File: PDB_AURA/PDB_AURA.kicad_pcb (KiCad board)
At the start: 4 copper layers, 50 x 50 mm, 76 parts, among them J100 XT30PW-M, J200 532617010, J201 XT30PW-F, J202 XT30PW-F, J203 XT30PW-F, J204 XT30PW-F, Q1 CSD18540Q5B, Q2 CSD18510Q5B, Q200 HSK10N06, Q201 HSK10N06, Q3 CSD18540Q5B, U1 LM25145RGYR, U2 LM74700, U200 LTV-217-B-G, U201 LTV-217-B-G, U202 INA219AIDCNR

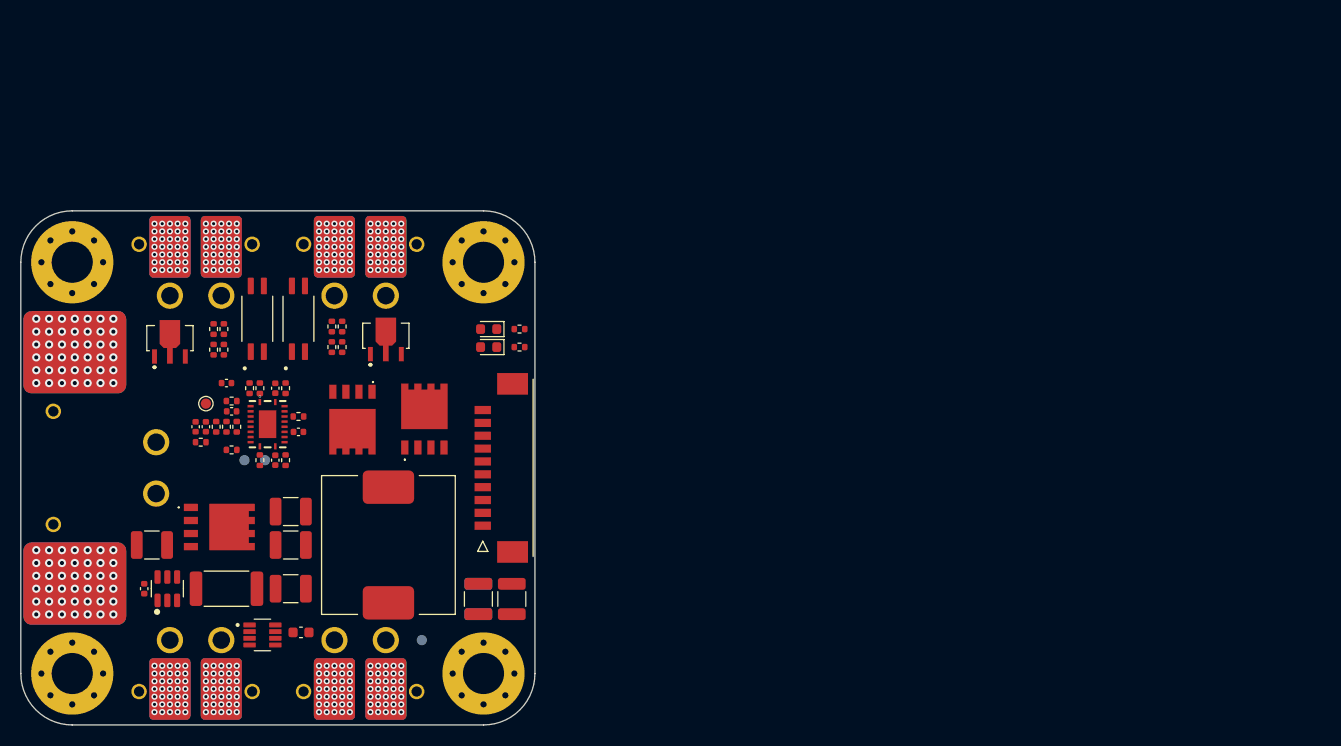
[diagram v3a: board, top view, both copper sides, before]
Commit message: Annotated schematic for PDB
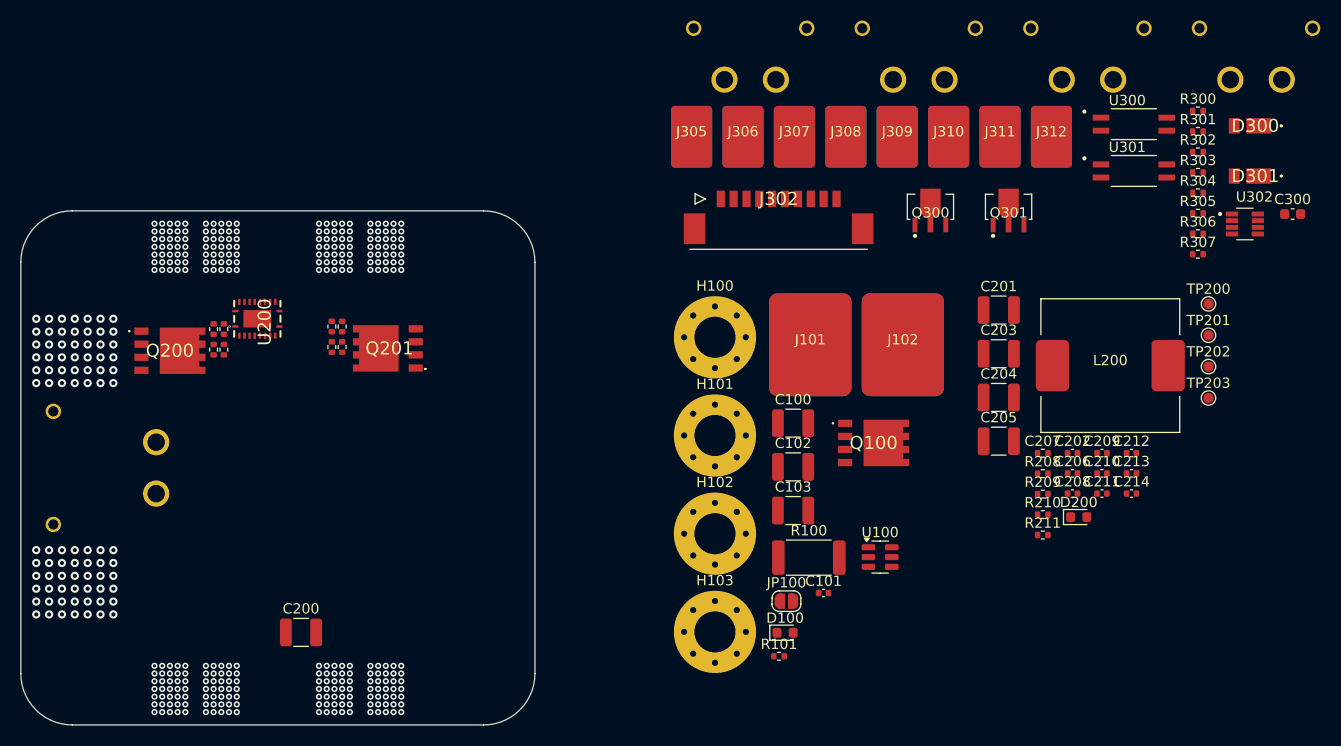
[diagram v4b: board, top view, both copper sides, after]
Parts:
- removed C1: 1n, Capacitor_SMD:C_0402_1005Metric
- removed C10: 47u, Capacitor_SMD:C_1210_3225Metric
- removed C11, C12, C14, C15, C16, C9: 22u, Capacitor_SMD:C_1210_3225Metric
- removed C2: 8n2, Capacitor_SMD:C_0402_1005Metric
- removed C3, C8: 100n, Capacitor_SMD:C_0402_1005Metric
- removed C4 (x2): 390p, Capacitor_SMD:C_0402_1005Metric
- removed C5: 100n, Resistor_SMD:R_0402_1005Metric
- removed C6: 2u2, Capacitor_SMD:C_0402_1005Metric
- removed C7: 10p, Capacitor_SMD:C_0402_1005Metric
- removed D1, D101: LED, LED_SMD:LED_0603_1608Metric
- removed H1, H2, H3, H4: MountingHole_Pad, MountingHole:MountingHole_4mm_Pad_Via
- removed J1, J2, J3, J4, J5, J6, J7, J8: ~, SOLDER_PAD:PWR_SOLDER_PAD
- removed J10, J9: ~, SOLDER_PAD:BAT_SOLDER_PAD
- removed J200: 532617010, 532617010:532617010
- removed J201, J202, J203, J204: XT30PW-F, XT30PWF:XT30PWF
- removed L1: 1u8, 125CDMCCDS-1R8MC:Untitled
- removed Q1, Q3: CSD18540Q5B, CSD18540Q5B:CSD18540Q5B
- removed Q2: CSD18510Q5B, CSD18510Q5B:CSD18540Q5BT
- removed R1: 18k, Resistor_SMD:R_0402_1005Metric
- removed R10: 9k1, Resistor_SMD:R_0402_1005Metric
- removed R11: 2R1, Resistor_SMD:R_0402_1005Metric
- removed R112, R13, R4, R8: 4k7, Resistor_SMD:R_0402_1005Metric
- removed R12: 0m5, Resistor_SMD:R_2512_6332Metric
- removed R2: 3k4, Resistor_SMD:R_0402_1005Metric
- removed R3: 1k47, Resistor_SMD:R_0402_1005Metric
- removed R5: 249R, Resistor_SMD:R_0402_1005Metric
- removed R6: 20k, Resistor_SMD:R_0402_1005Metric
- removed R7: 576R, Resistor_SMD:R_0402_1005Metric
- removed R9: 35k7, Resistor_SMD:R_0402_1005Metric
- removed TP1, TP2, TP3, TP4: TestPoint, TestPoint:TestPoint_Pad_D1.0mm
- removed U1: LM25145RGYR, LM24145RGYR:RGY0020B
- removed U2: LM74700, Package_TO_SOT_SMD:SOT-23-6
- removed U201: LTV-217-B-G, LTV-217-B-G:SOIC127P700X210-4N
- removed U202: INA219AIDCNR, INA219AIDCNR:SOT65P280X145-8N
- added C100: 22u, Capacitor_SMD:C_1210_3225Metric, F.Cu at (125.1, 70.7)
- added C101: 47n, Capacitor_SMD:C_0402_1005Metric, F.Cu at (128.1, 87.2)
- added C102: 22u, Capacitor_SMD:C_1210_3225Metric, F.Cu at (125.1, 74.9)
- added C103: 22u, Capacitor_SMD:C_1210_3225Metric, F.Cu at (125.1, 79.2)
- added C201: 22u, Capacitor_SMD:C_1210_3225Metric, F.Cu at (145.1, 59.6)
- added C202: 100n, Capacitor_SMD:C_0402_1005Metric, F.Cu at (152.3, 73.6)
- added C203: 22u, Capacitor_SMD:C_1210_3225Metric, F.Cu at (145.1, 63.9)
- added C204: 22u, Capacitor_SMD:C_1210_3225Metric, F.Cu at (145.1, 68.2)
- added C205: 22u, Capacitor_SMD:C_1210_3225Metric, F.Cu at (145.1, 72.4)
- added C206: 100n, Capacitor_SMD:C_0402_1005Metric, F.Cu at (152.3, 75.5)
- added C207: 100n, Resistor_SMD:R_0402_1005Metric, F.Cu at (149.4, 73.6)
- added C208: 100n, Capacitor_SMD:C_0402_1005Metric, F.Cu at (152.3, 77.5)
- added C209: 2u2, Capacitor_SMD:C_0402_1005Metric, F.Cu at (155.2, 73.6)
- added C210: 10p, Capacitor_SMD:C_0402_1005Metric, F.Cu at (155.2, 75.5)
- added C211: 100n, Capacitor_SMD:C_0402_1005Metric, F.Cu at (155.2, 77.5)
- added C212: 1n, Capacitor_SMD:C_0402_1005Metric, F.Cu at (158.0, 73.6)
- added C213: 8n2, Capacitor_SMD:C_0402_1005Metric, F.Cu at (158.0, 75.5)
- added C214: 390p, Capacitor_SMD:C_0402_1005Metric, F.Cu at (158.0, 77.5)
- added C300: 100n, Capacitor_SMD:C_0603_1608Metric, F.Cu at (173.7, 50.3)
- added D100: LED, LED_SMD:LED_0603_1608Metric, F.Cu at (124.3, 91.0)
- added D200: LED, LED_SMD:LED_0603_1608Metric, F.Cu at (152.9, 79.8)
- added D300: SBR3M30P17, SBR3M30P17:SBR3M30P17, F.Cu at (169.5, 41.7)
- added D301: SBR3M30P17, SBR3M30P17:SBR3M30P17, F.Cu at (169.5, 46.6)
- added H100: MountingHole_Pad, MountingHole:MountingHole_4mm_Pad_Via, F.Cu at (117.5, 62.3)
- added H101: MountingHole_Pad, MountingHole:MountingHole_4mm_Pad_Via, F.Cu at (117.5, 71.8)
- added H102: MountingHole_Pad, MountingHole:MountingHole_4mm_Pad_Via, F.Cu at (117.5, 81.4)
- added H103: MountingHole_Pad, MountingHole:MountingHole_4mm_Pad_Via, F.Cu at (117.5, 91.0)
- added J101: ~, SOLDER_PAD:BAT_SOLDER_PAD, F.Cu at (126.8, 63.0)
- added J102: ~, SOLDER_PAD:BAT_SOLDER_PAD, F.Cu at (135.8, 63.0)
- added J300: XT30PW-F, XT30PWF:XT30PWF, F.Cu at (118.4, 37.2)
- added J301: XT30PW-F, XT30PWF:XT30PWF, F.Cu at (134.8, 37.2)
- added J302: 532617010, 532617010:532617010, F.Cu at (123.7, 48.8)
- added J303: XT30PW-F, XT30PWF:XT30PWF, F.Cu at (151.2, 37.2)
- added J304: XT30PW-F, XT30PWF:XT30PWF, F.Cu at (167.6, 37.2)
- added J305: ~, SOLDER_PAD:PWR_SOLDER_PAD, F.Cu at (115.2, 42.8)
- added J306: ~, SOLDER_PAD:PWR_SOLDER_PAD, F.Cu at (120.2, 42.8)
- added J307: ~, SOLDER_PAD:PWR_SOLDER_PAD, F.Cu at (125.2, 42.8)
- added J308: ~, SOLDER_PAD:PWR_SOLDER_PAD, F.Cu at (130.2, 42.8)
- added J309: ~, SOLDER_PAD:PWR_SOLDER_PAD, F.Cu at (135.2, 42.8)
- added J310: ~, SOLDER_PAD:PWR_SOLDER_PAD, F.Cu at (140.2, 42.8)
- added J311: ~, SOLDER_PAD:PWR_SOLDER_PAD, F.Cu at (145.2, 42.8)
- added J312: ~, SOLDER_PAD:PWR_SOLDER_PAD, F.Cu at (150.2, 42.8)
- added JP100: SolderJumper_2_Open, Jumper:SolderJumper-2_P1.3mm_Open_RoundedPad1.0x1.5mm, F.Cu at (124.5, 88.0)
- added L200: 1u8, 125CDMCCDS-1R8MC:Untitled, F.Cu at (156.0, 65.0)
- added Q100: CSD18540Q5B, CSD18540Q5B:CSD18540Q5B, F.Cu at (132.9, 72.6)
- added Q300: HSK10N06, HSK10N06:HSK10N06, F.Cu at (138.5, 50.8)
- added Q301: HSK10N06, HSK10N06:HSK10N06, F.Cu at (146.1, 50.8)
- added R100: 0m5, Resistor_SMD:R_2512_6332Metric, F.Cu at (126.6, 83.7)
- added R101: 4k7, Resistor_SMD:R_0402_1005Metric, F.Cu at (123.7, 93.3)
- added R208: 4k7, Resistor_SMD:R_0402_1005Metric, F.Cu at (149.4, 75.6)
- added R209: 4k7, Resistor_SMD:R_0402_1005Metric, F.Cu at (149.4, 77.5)
- added R210: 576R, Resistor_SMD:R_0402_1005Metric, F.Cu at (149.4, 79.5)
- added R211: 4k7, Resistor_SMD:R_0402_1005Metric, F.Cu at (149.4, 81.5)
- added R300: 10k, Resistor_SMD:R_0402_1005Metric, F.Cu at (164.5, 40.3)
- added R301: 220R, Resistor_SMD:R_0402_1005Metric, F.Cu at (164.5, 42.3)
- added R302: 10k, Resistor_SMD:R_0402_1005Metric, F.Cu at (164.5, 44.3)
- added R303: 100R, Resistor_SMD:R_0402_1005Metric, F.Cu at (164.5, 46.3)
- added R304: 10k, Resistor_SMD:R_0402_1005Metric, F.Cu at (164.5, 48.2)
- added R305: 220R, Resistor_SMD:R_0402_1005Metric, F.Cu at (164.5, 50.2)
- added R306: 10k, Resistor_SMD:R_0402_1005Metric, F.Cu at (164.5, 52.2)
- added R307: 100R, Resistor_SMD:R_0402_1005Metric, F.Cu at (164.5, 54.2)
- added TP200: TestPoint, TestPoint:TestPoint_Pad_D1.0mm, F.Cu at (165.5, 59.0)
- added TP201: TestPoint, TestPoint:TestPoint_Pad_D1.0mm, F.Cu at (165.5, 62.1)
- added TP202: TestPoint, TestPoint:TestPoint_Pad_D1.0mm, F.Cu at (165.5, 65.2)
- added TP203: TestPoint, TestPoint:TestPoint_Pad_D1.0mm, F.Cu at (165.5, 68.2)
- added U100: LM74700, Package_TO_SOT_SMD:SOT-23-6, F.Cu at (133.6, 83.7)
- added U300: LTV-217-B-G, LTV-217-B-G:SOIC127P700X210-4N, F.Cu at (158.2, 41.6)
- added U301: LTV-217-B-G, LTV-217-B-G:SOIC127P700X210-4N, F.Cu at (158.2, 46.1)
- added U302: INA219AIDCNR, INA219AIDCNR:SOT65P280X145-8N, F.Cu at (169.1, 51.3)
- C200: value 100n -> 47u; footprint Capacitor_SMD:C_0603_1608Metric -> Capacitor_SMD:C_1210_3225Metric
- Q200: value HSK10N06 -> CSD18540Q5B; footprint HSK10N06:HSK10N06 -> CSD18540Q5B:CSD18540Q5B
- Q201: value HSK10N06 -> CSD18510Q5B; footprint HSK10N06:HSK10N06 -> CSD18510Q5B:CSD18540Q5BT
- R200: value 10k -> 2R1
- R201: value 470R -> 35k7
- R202: value 10k -> 9k1
- R203: value 100R -> 20k
- R204: value 10k -> 249R
- R205: value 470R -> 3k4
- R206: value 10k -> 18k
- R207: value 100R -> 1k47
- U200: value LTV-217-B-G -> LM25145RGYR; footprint LTV-217-B-G:SOIC127P700X210-4N -> LM24145RGYR:RGY0020B
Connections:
- C200 pad 1: +3V3 -> +BATT_FILT
- Q200 pad 1: /200_Connectors/VGS_CH1_R -> /200_Buck_Regulator/5V_HO
- Q200 pad 2: /200_Connectors/VBAT_CH1 -> +BATT_FILT
- Q200 pad 3: GND -> /200_Buck_Regulator/5V_SW
- Q201 pad 1: /200_Connectors/VGS_CH2_R -> /200_Buck_Regulator/5V_LO
- Q201 pad 2: /200_Connectors/VBAT_CH2 -> /200_Buck_Regulator/5V_SW
- R200 pad 1: GND -> /200_Buck_Regulator/5V_VIN
- R200 pad 2: MSFT_1 -> +BATT_FILT
- R201 pad 1: /200_Connectors/MSFT_1_R -> /200_Buck_Regulator/5V_EN
- R201 pad 2: MSFT_1 -> +BATT_FILT
- R202 pad 2: /200_Connectors/VGS_CH1 -> /200_Buck_Regulator/5V_EN
- R203 pad 1: /200_Connectors/VGS_CH1_R -> /200_Buck_Regulator/5V_SYNCIN
- R203 pad 2: /200_Connectors/VGS_CH1 -> +5V_VCC
- R204 pad 1: GND -> /200_Buck_Regulator/5V_FB_RC
- R204 pad 2: MSFT_2 -> +5V
- R205 pad 1: /200_Connectors/MSFT_2_R -> GND
- R205 pad 2: MSFT_2 -> /200_Buck_Regulator/5V_FB
- R206 pad 1: GND -> /200_Buck_Regulator/5V_FB
- R206 pad 2: /200_Connectors/VGS_CH2 -> +5V
- R207 pad 1: /200_Connectors/VGS_CH2_R -> /200_Buck_Regulator/5V_FB
- R207 pad 2: /200_Connectors/VGS_CH2 -> /200_Buck_Regulator/COMP_FB_R
- U200 pad 1: /200_Connectors/MSFT_1_R -> /200_Buck_Regulator/5V_EN
- U200 pad 2: GND -> /200_Buck_Regulator/5V_RT
- U200 pad 3: /200_Connectors/VGS_CH1 -> /200_Buck_Regulator/5V_SS
- U200 pad 4: +5V -> /200_Buck_Regulator/COMP_FB_C

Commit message: Second Layout Attempt
Renamed all components and placed them all.
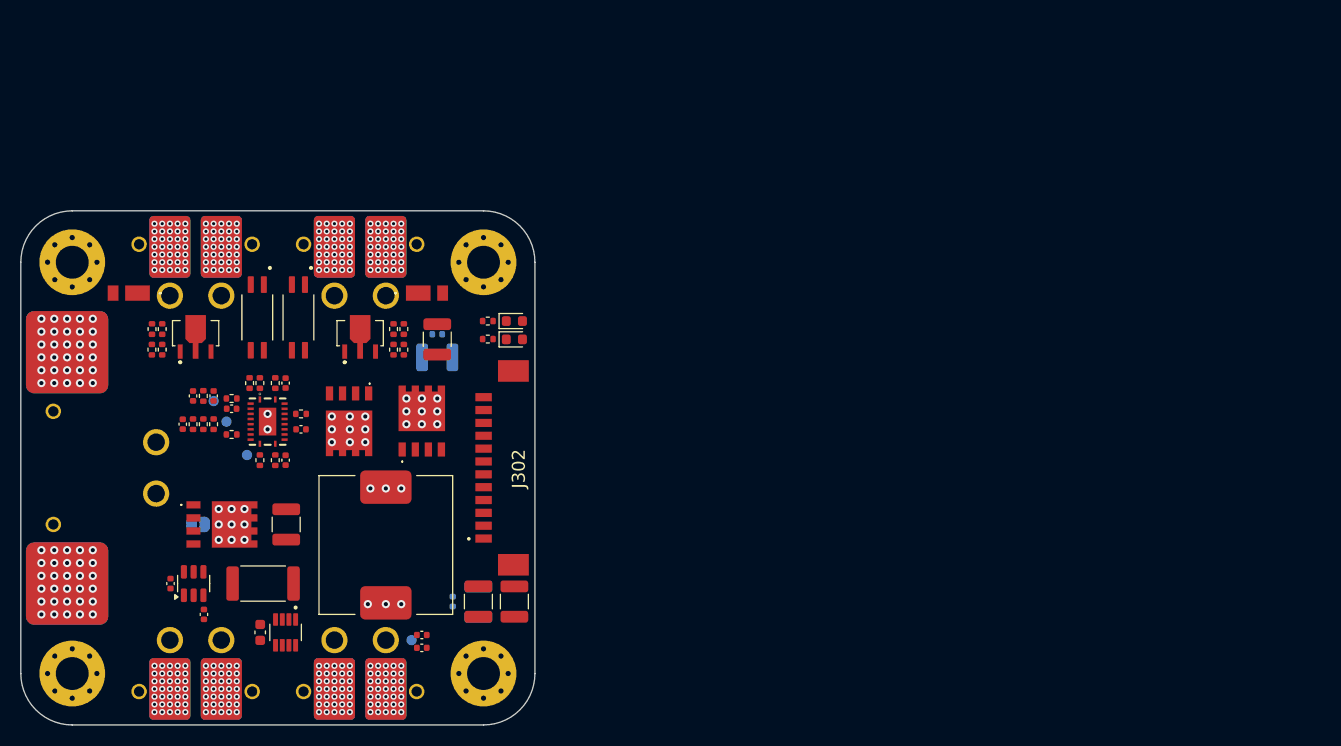
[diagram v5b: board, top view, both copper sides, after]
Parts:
- removed C100, C103: 22u, Capacitor_SMD:C_1210_3225Metric
- removed C206: 100n, Capacitor_SMD:C_0402_1005Metric
- added C104: 22n, Capacitor_SMD:C_0402_1005Metric, F.Cu at (67.8, 89.2)
- added C215: 100n, Capacitor_SMD:C_0402_1005Metric, B.Cu at (92.0, 88.0)
- added C216: 22u, Capacitor_SMD:C_1210_3225Metric, B.Cu at (94.5, 88.0)
- added C217: 100n, Capacitor_SMD:C_0402_1005Metric, B.Cu at (90.5, 62.0)
- added C218: 1u, Capacitor_SMD:C_0402_1005Metric, B.Cu at (90.5, 61.0)
- C102: value 22u -> 47u
- C201: value 22u -> 47u; moved to B.Cu
- C203: value 22u -> 1u; footprint Capacitor_SMD:C_1210_3225Metric -> Capacitor_SMD:C_0402_1005Metric
- H100, H101, H102, H103: footprint MountingHole:MountingHole_4mm_Pad_Via -> MountingHole:MountingHole_3.2mm_M3_Pad_Via
- J302: value 532617010 -> 532617012; footprint 532617010:532617010 -> 532611271:53261-1271
- J305, J306, J307, J308, J309, J310, J311, J312, JP100, TP200, TP201, TP202, TP203: moved to B.Cu
- moved D301 109.6 mm to (60.5, 58.0)
- moved C300 108.3 mm to (73.3, 91.0), turned to -90 degrees
- moved R300 104.3 mm to (62.8, 63.5), turned to -90 degrees
- moved R302 103.2 mm to (62.8, 61.5), turned to 90 degrees
- moved R301 102.9 mm to (63.8, 63.5), turned to -90 degrees
- moved R303 101.9 mm to (63.8, 61.5), turned to 90 degrees
- moved U302 101.4 mm to (75.8, 91.0), turned to -90 degrees
- moved J312 101.2 mm to (64.5, 96.5), turned to 180 degrees
- moved J304 98.6 mm to (85.5, 91.8), turned to 180 degrees
- moved J303 98.2 mm to (69.5, 91.8), turned to 180 degrees
- moved TP201 97.0 mm to (68.8, 68.5), turned to 180 degrees
- moved TP203 95.5 mm to (70.0, 70.5), turned to 180 degrees
- moved TP202 93.9 mm to (72.0, 73.8), turned to 180 degrees
- moved J311 92.8 mm to (69.5, 96.5), turned to 180 degrees
- moved C213 92.4 mm to (65.8, 70.8), turned to 90 degrees
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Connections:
- C202 pad 1: +BATT_FILT -> +5V
- J302 pad 11: (no net) -> GND
- J302 pad 12: (no net) -> GND
- J302 pad 3: +3V3 -> +5V
- J302 pad 4: SCL -> +3V3
- J302 pad 5: SDA -> SCL
- J302 pad 6: GND -> SDA
- J302 pad 7: MSFT_1 -> GND
- J302 pad 8: MSFT_2 -> MSFT_1
- J302 pad 9: GND -> MSFT_2
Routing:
- net INA_IN+: vias 0 -> 9
- net GND: vias 182 -> 172
- net /200_Buck_Regulator/5V_SW: vias 0 -> 12
- net +BATT_FILT: vias 140 -> 149
- net +BATT: vias 42 -> 30
- net +5V: vias 0 -> 3

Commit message: Started Routing
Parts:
- C201, C215, C216, C217: moved to F.Cu
- J302: moved to B.Cu
- moved C216 11.8 mm to (95.5, 76.2), turned to 0 degrees
- moved C202 9.55 mm to (95.5, 85.5)
- moved D100 8.63 mm to (96.5, 71.0)
- moved D200 8.63 mm to (96.5, 69.2)
- moved R101 8.63 mm to (93.9, 71.0)
- moved R211 8.63 mm to (93.9, 69.2)
- moved C205 8.31 mm to (95.5, 79.8), turned to 0 degrees
- moved C203 8.05 mm to (95.5, 86.5)
- moved C217 5.77 mm to (96.2, 62.5), turned to 90 degrees
- moved C104 5.71 mm to (64.0, 85.0), turned to 180 degrees
- moved C204 5.37 mm to (95.5, 83.2), turned to 0 degrees
- moved TP200 4.51 mm to (85.5, 88.0)
- moved C201 3.91 mm to (94.0, 62.5), turned to 90 degrees
- moved C215 3.54 mm to (95.5, 87.5), turned to 0 degrees
- moved TP202 2.02 mm to (70.0, 73.5)
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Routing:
- net GND: vias 172 -> 162
- net /300_Connectors/VBAT_CH2: vias 0 -> 2
- net /300_Connectors/VBAT_CH1: vias 0 -> 2
- net +BATT_FILT: vias 149 -> 153
- net +BATT: vias 30 -> 20
- added copper zone on F.Cu, net +5V
- added copper zone on F.Cu, net +BATT_FILT
- added copper zone on F.Cu, net /200_Buck_Regulator/5V_SW
- added copper zone on B.Cu, net GND
- added copper zone on F.Cu, net GND
- added copper zone on In1.Cu, net GND
